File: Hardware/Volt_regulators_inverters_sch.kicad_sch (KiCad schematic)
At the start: 14 parts, among them IC1 MCP1754ST-3302E_DB, U11 LM2665M6, U12 TLV77333PDQNR, U6 TPS73133DBV, U7 TPS72325DBV, U8 TPS73201DCQ

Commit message: schematics redone, TODO: Pcb component placement
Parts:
- added C45, C46: 10 u, Capacitor_SMD:C_0603_1608Metric, symbol Device:C_Small
- IC1: footprint SOT230P700X180-4N -> mcp1754:SOT230P700X180-4N
- U12: footprint X2SON_DQN4_TEX -> tlv77333:X2SON_DQN4_TEX
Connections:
- net AVSS: now also C46.1
- net GNDA: now also C46.2
- net at U11.3 (CAP-): now also C45.2
- net at U11.6 (CAP+): now also C45.1
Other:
- note added: "3.3V LDO REG#2 e #3"
- note removed: "3.3V LDO REG#2"
- moved on the sheet: U12
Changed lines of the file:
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@@
 	(paper "A4")
+	(junction
+		(at 60.96 48.26)
+		(diameter 0)
+		(color 0 0 0 0)
+	)
 	(junction
 		(at 31.75 124.46)
@@
 	)
 	(junction
+		(at 90.17 38.1)
+		(diameter 0)
+		(color 0 0 0 0)
+	)
+	(junction
 		(at 45.72 72.39)
 		(diameter 0)
@@
 	(wire
 		(pts
+			(xy 90.17 48.26) (xy 90.17 45.72)
+		)
+		(stroke
+			(width 0)
+			(type default)
+		)
+	)
+	(wire
+		(pts
 			(xy 49.53 74.93) (xy 49.53 72.39)
 		)
@@
 	(wire
 		(pts
-			(xy 78.74 38.1) (xy 71.12 38.1)
+			(xy 78.74 45.72) (xy 71.12 45.72)
+		)
+		(stroke
+			(width 0)
+			(type default)
+		)
+	)
+	(wire
+		(pts
+			(xy 93.98 38.1) (xy 90.17 38.1)
 		)
 		(stroke
@@
 	(wire
 		(pts
+			(xy 90.17 40.64) (xy 90.17 38.1)
+		)
+		(stroke
+			(width 0)
+			(type default)
+		)
+	)
+	(wire
+		(pts
 			(xy 31.75 137.16) (xy 55.88 137.16)
 		)
@@
 	(wire
 		(pts
+			(xy 71.12 40.64) (xy 78.74 40.64)
+		)
+		(stroke
+			(width 0)
+			(type default)
+		)
+	)
+	(wire
+		(pts
 			(xy 80.01 137.16) (xy 71.12 137.16)
 		)
@@
 	(wire
 		(pts
+			(xy 90.17 38.1) (xy 71.12 38.1)
+		)
+		(stroke
+			(width 0)
+			(type default)
+		)
+	)
+	(wire
+		(pts
 			(xy 60.96 82.55) (xy 74.93 82.55)
 		)
@@
 	(wire
 		(pts
+			(xy 71.12 45.72) (xy 71.12 43.18)
+		)
+		(stroke
+			(width 0)
+			(type default)
+		)
+	)
+	(wire
+		(pts
 			(xy 31.75 124.46) (xy 45.72 124.46)
 		)
@@
 		(pts
 			(xy 74.93 80.01) (xy 74.93 82.55)
+		)
+		(stroke
+			(width 0)
+			(type default)
+		)
+	)
+	(wire
+		(pts
+			(xy 60.96 48.26) (xy 90.17 48.26)
 		)
 		(stroke
@@
 		)
 	)
-	(text "3.3V LDO REG#2\n\n"
-		(exclude_from_sim no)
-		(at 163.068 25.146 0)
+	(text "3.3V LDO REG#2 e #3\n\n\n"
+		(exclude_from_sim no)
+		(at 167.386 33.528 0)
 		(effects
 			(font
@@
 	(global_label "AVSS"
 		(shape input)
-		(at 78.74 38.1 0)
+		(at 93.98 38.1 0)
 		(fields_autoplaced yes)
 		(effects
@@
 		)
 		(property "Intersheetrefs" "${INTERSHEET_REFS}"
-			(at 86.3214 38.1 0)
+			(at 101.5614 38.1 0)
 			(effects
 				(font
@@
 	(symbol
 		(lib_id "Device:C_Small")
+		(at 78.74 43.18 0)
+		(unit 1)
+		(exclude_from_sim no)
+		(in_bom yes)
+		(on_board yes)
+		(dnp no)
+		(fields_autoplaced yes)
+		(property "Reference" "C45"
+			(at 81.28 41.9162 0)
+			(effects
+				(font
+					(size 1.27 1.27)
+				)
+				(justify left)
+			)
+		)
+		(property "Value" "10 u"
+			(at 81.28 44.4562 0)
+			(effects
+				(font
+					(size 1.27 1.27)
+				)
+				(justify left)
+			)
+		)
+		(property "Footprint" "Capacitor_SMD:C_0603_1608Metric"
+			(at 78.74 43.18 0)
+			(effects
+				(font
+					(size 1.27 1.27)
+				)
+				(hide yes)
+			)
+		)
+		(property "Datasheet" "~"
+			(at 78.74 43.18 0)
+			(effects
+				(font
+					(size 1.27 1.27)
+				)
+				(hide yes)
+			)
+		)
+		(property "Description" ""
+			(at 78.74 43.18 0)
+			(effects
+				(font
+					(size 1.27 1.27)
+				)
+				(hide yes)
+			)
+		)
+		(pin "2"
+		)
+		(pin "1"
+		)
+		(instances
+			(project "bioamplifier"
+				(path "/59c54cdb-19a2-4654-a4c9-f1907d038780/db58efb1-7103-4a17-b794-0e1a9c461960"
+					(reference "C45")
+					(unit 1)
+				)
+			)
+		)
+	)
+	(symbol
+		(lib_id "Device:C_Small")
 		(at 45.72 77.47 0)
 		(unit 1)
@@
 		(on_board yes)
 		(dnp no)
-		(fields_autoplaced yes)
 		(property "Reference" "C29"
-			(at 78.486 76.2063 0)
+			(at 73.66 75.946 0)
 			(effects
 				(font
@@
 		)
 		(property "Value" "0.1 nF"
-			(at 78.486 78.7463 0)
+			(at 72.644 79.248 0)
 			(effects
 				(font
@@
 			)
 		)
-		(property "Footprint" "SOT230P700X180-4N"
+		(property "Footprint" "mcp1754:SOT230P700X180-4N"
 			(at 196.85 136.83 0)
 			(effects
@@
 	(symbol
 		(lib_id "tlv77333:TLV77333PDQNR")
-		(at 166.37 80.01 0)
+		(at 207.01 41.91 0)
 		(unit 1)
 		(exclude_from_sim no)
@@
 		(fields_autoplaced yes)
 		(property "Reference" "U12"
-			(at 186.69 69.85 0)
+			(at 227.33 31.75 0)
 			(effects
 				(font
@@
 		)
 		(property "Value" "TLV77333PDQNR"
-			(at 186.69 72.39 0)
+			(at 227.33 34.29 0)
 			(effects
 				(font
@@
 			)
 		)
-		(property "Footprint" "X2SON_DQN4_TEX"
-			(at 166.37 80.01 0)
+		(property "Footprint" "tlv77333:X2SON_DQN4_TEX"
+			(at 207.01 41.91 0)
 			(effects
 				(font
@@
 		)
 		(property "Datasheet" "TLV77333PDQNR"
-			(at 166.37 80.01 0)
+			(at 207.01 41.91 0)
 			(effects
 				(font
@@
 		)
 		(property "Description" ""
-			(at 166.37 80.01 0)
+			(at 207.01 41.91 0)
 			(effects
 				(font
@@
 	(symbol
 		(lib_id "Device:C_Small")
+		(at 90.17 43.18 0)
+		(unit 1)
+		(exclude_from_sim no)
+		(in_bom yes)
+		(on_board yes)
+		(dnp no)
+		(fields_autoplaced yes)
+		(property "Reference" "C46"
+			(at 92.71 41.9162 0)
+			(effects
+				(font
+					(size 1.27 1.27)
+				)
+				(justify left)
+			)
+		)
+		(property "Value" "10 u"
+			(at 92.71 44.4562 0)
+			(effects
+				(font
+					(size 1.27 1.27)
+				)
+				(justify left)
+			)
+		)
+		(property "Footprint" "Capacitor_SMD:C_0603_1608Metric"
+			(at 90.17 43.18 0)
+			(effects
+				(font
+					(size 1.27 1.27)
+				)
+				(hide yes)
+			)
+		)
+		(property "Datasheet" "~"
+			(at 90.17 43.18 0)
+			(effects
+				(font
+					(size 1.27 1.27)
+				)
+				(hide yes)
+			)
+		)
+		(property "Description" ""
+			(at 90.17 43.18 0)
+			(effects
+				(font
+					(size 1.27 1.27)
+				)
+				(hide yes)
+			)
+		)
+		(pin "2"
+		)
+		(pin "1"
+		)
+		(instances
+			(project "bioamplifier"
+				(path "/59c54cdb-19a2-4654-a4c9-f1907d038780/db58efb1-7103-4a17-b794-0e1a9c461960"
+					(reference "C46")
+					(unit 1)
+				)
+			)
+		)
+	)
+	(symbol
+		(lib_id "Device:C_Small")
 		(at 147.5241 126.3073 0)
 		(unit 1)
@@
 		(on_board yes)
 		(dnp no)
-		(fields_autoplaced yes)
 		(property "Reference" "C41"
-			(at 84.836 76.2063 0)
+			(at 80.01 75.946 0)
 			(effects
 				(font
@@
 		)
 		(property "Value" "0.1 nF"
-			(at 84.836 78.7463 0)
-			(effects
-				(font
+			(at 79.756 79.248 0)
+			(effects
+				(font

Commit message: changes to pcb and schematics
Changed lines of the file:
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@@
-	(wire
-		(pts
-			(xy 230.124 119.634) (xy 230.124 119.38)
-		)
-		(stroke
-			(width 0)
-			(type default)
-		)
-	)
 	(wire
 		(pts
@@
 	(wire
 		(pts
+			(xy 220.98 119.38) (xy 231.14 119.38)
+		)
+		(stroke
+			(width 0)
+			(type default)
+		)
+	)
+	(wire
+		(pts
 			(xy 45.72 82.55) (xy 60.96 82.55)
 		)
@@
 	(wire
 		(pts
-			(xy 148.844 121.92) (xy 160.02 121.92)
-		)
-		(stroke
-			(width 0)
-			(type default)
-		)
-	)
-	(wire
-		(pts
 			(xy 45.72 72.39) (xy 45.72 74.93)
 		)
@@
 	(wire
 		(pts
-			(xy 230.632 119.634) (xy 230.124 119.634)
-		)
-		(stroke
-			(width 0)
-			(type default)
-		)
-	)
-	(wire
-		(pts
 			(xy 81.28 82.55) (xy 74.93 82.55)
 		)
@@
 		(pts
 			(xy 60.96 48.26) (xy 90.17 48.26)
-		)
-		(stroke
-			(width 0)
-			(type default)
-		)
-	)
-	(wire
-		(pts
-			(xy 230.124 119.38) (xy 220.98 119.38)
 		)
 		(stroke
@@
 		)
 	)
-	(label "5V_UNREG"
-		(at 143.51 119.38 0)
-		(fields_autoplaced yes)
-		(effects
-			(font
-				(size 1.27 1.27)
-			)
-			(justify left bottom)
-		)
-	)
-	(label "AVDD"
-		(at 148.844 121.92 0)
-		(fields_autoplaced yes)
-		(effects
-			(font
-				(size 1.27 1.27)
-			)
-			(justify left bottom)
-		)
-	)
-	(label "5V_UNREG"
-		(at 230.632 119.634 0)
-		(fields_autoplaced yes)
-		(effects
-			(font
-				(size 1.27 1.27)
-			)
-			(justify left bottom)
-		)
-	)
 	(global_label "3.3V_UNREG"
 		(shape input)
@@
 		)
 	)
+	(global_label "5V_UNREG"
+		(shape input)
+		(at 231.14 119.38 0)
+		(fields_autoplaced yes)
+		(effects
+			(font
+				(size 1.27 1.27)
+			)
+			(justify left)
+		)
+		(property "Intersheetrefs" "${INTERSHEET_REFS}"
+			(at 243.7409 119.38 0)
+			(effects
+				(font
+					(size 1.27 1.27)
+				)
+				(justify left)
+				(hide yes)
+			)
+		)
+	)
 	(global_label "DVDD"
 		(shape input)
@@
 		)
 	)
+	(global_label "AVDD"
+		(shape input)
+		(at 160.02 121.92 180)
+		(fields_autoplaced yes)
+		(effects
+			(font
+				(size 1.27 1.27)
+			)
+			(justify right)
+		)
+		(property "Intersheetrefs" "${INTERSHEET_REFS}"
+			(at 152.3176 121.92 0)
+			(effects
+				(font
+					(size 1.27 1.27)
+				)
+				(justify right)
+				(hide yes)
+			)
+		)
+	)
 	(global_label "-2.5V_UNREG"
 		(shape input)
@@
 				(hide yes)
 			)
+		)
+	)
+	(global_label "5V_UNREG"
+		(shape input)
+		(at 143.51 119.38 180)
+		(fields_autoplaced yes)
+		(effects
+			(font
+				(size 1.27 1.27)
+			)
+			(justify right)
+		)
+		(property "Intersheetrefs" "${INTERSHEET_REFS}"
+			(at 130.9091 119.38 0)
+			(effects
+				(font
+					(size 1.27 1.27)
+				)
+				(justify right)
+				(hide yes)
+			)

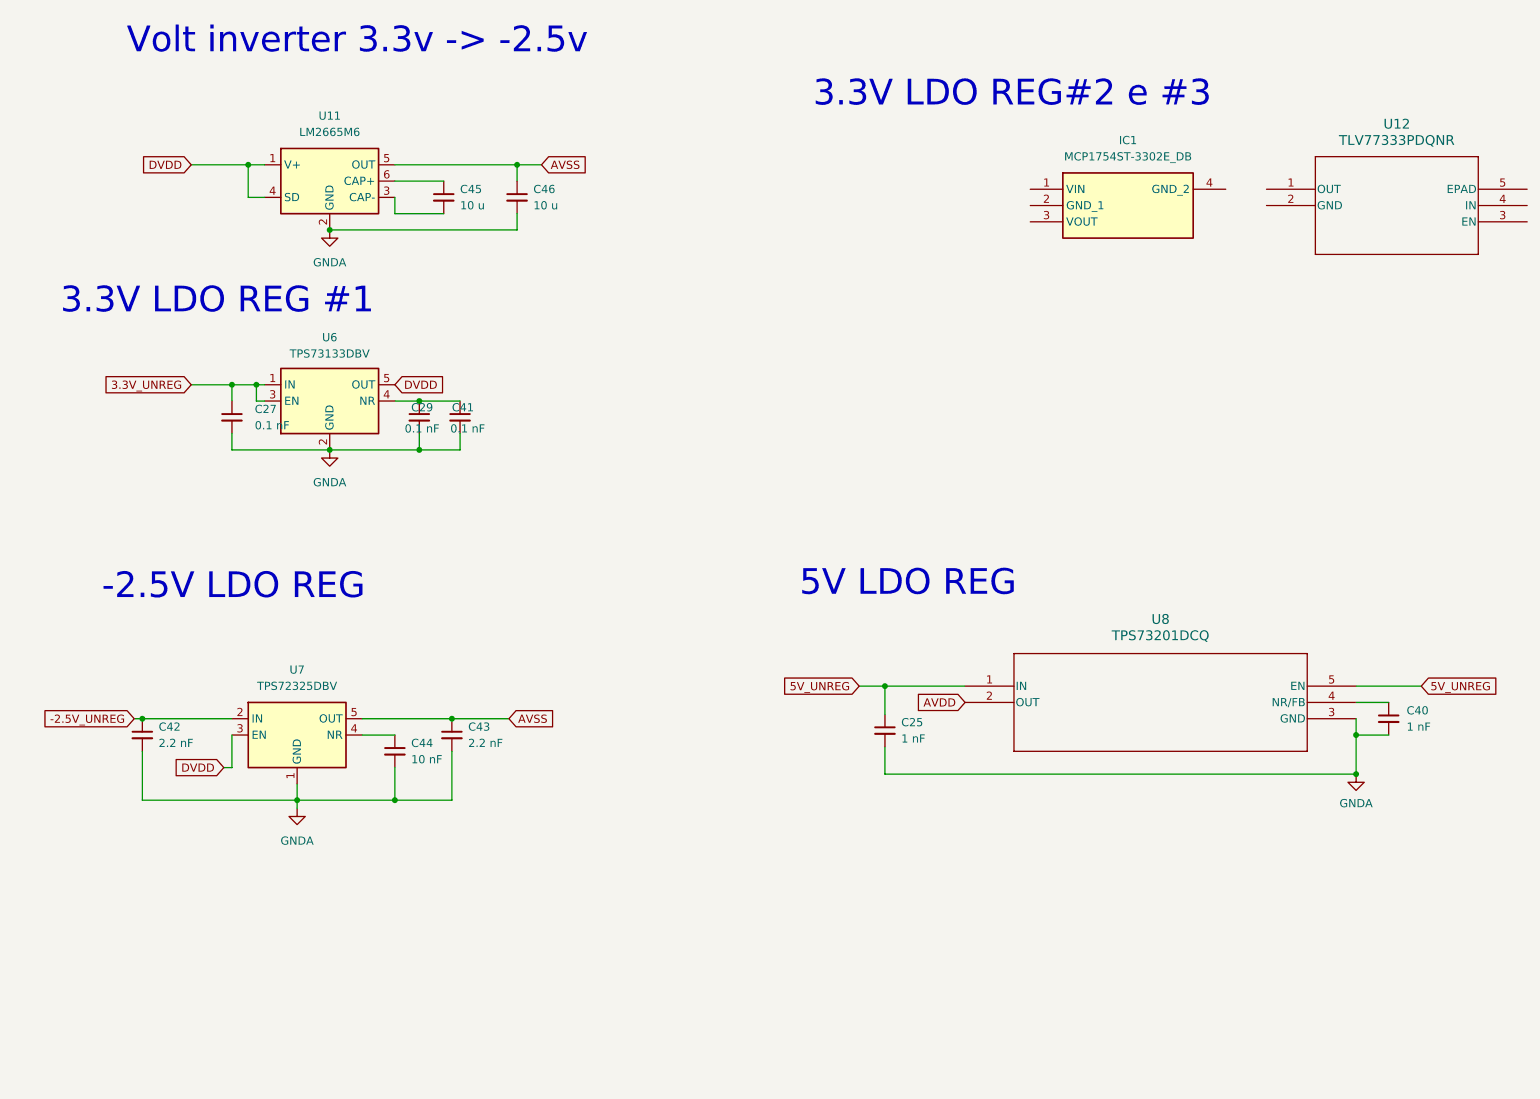
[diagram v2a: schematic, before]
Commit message: removed 5V LDO Regulator
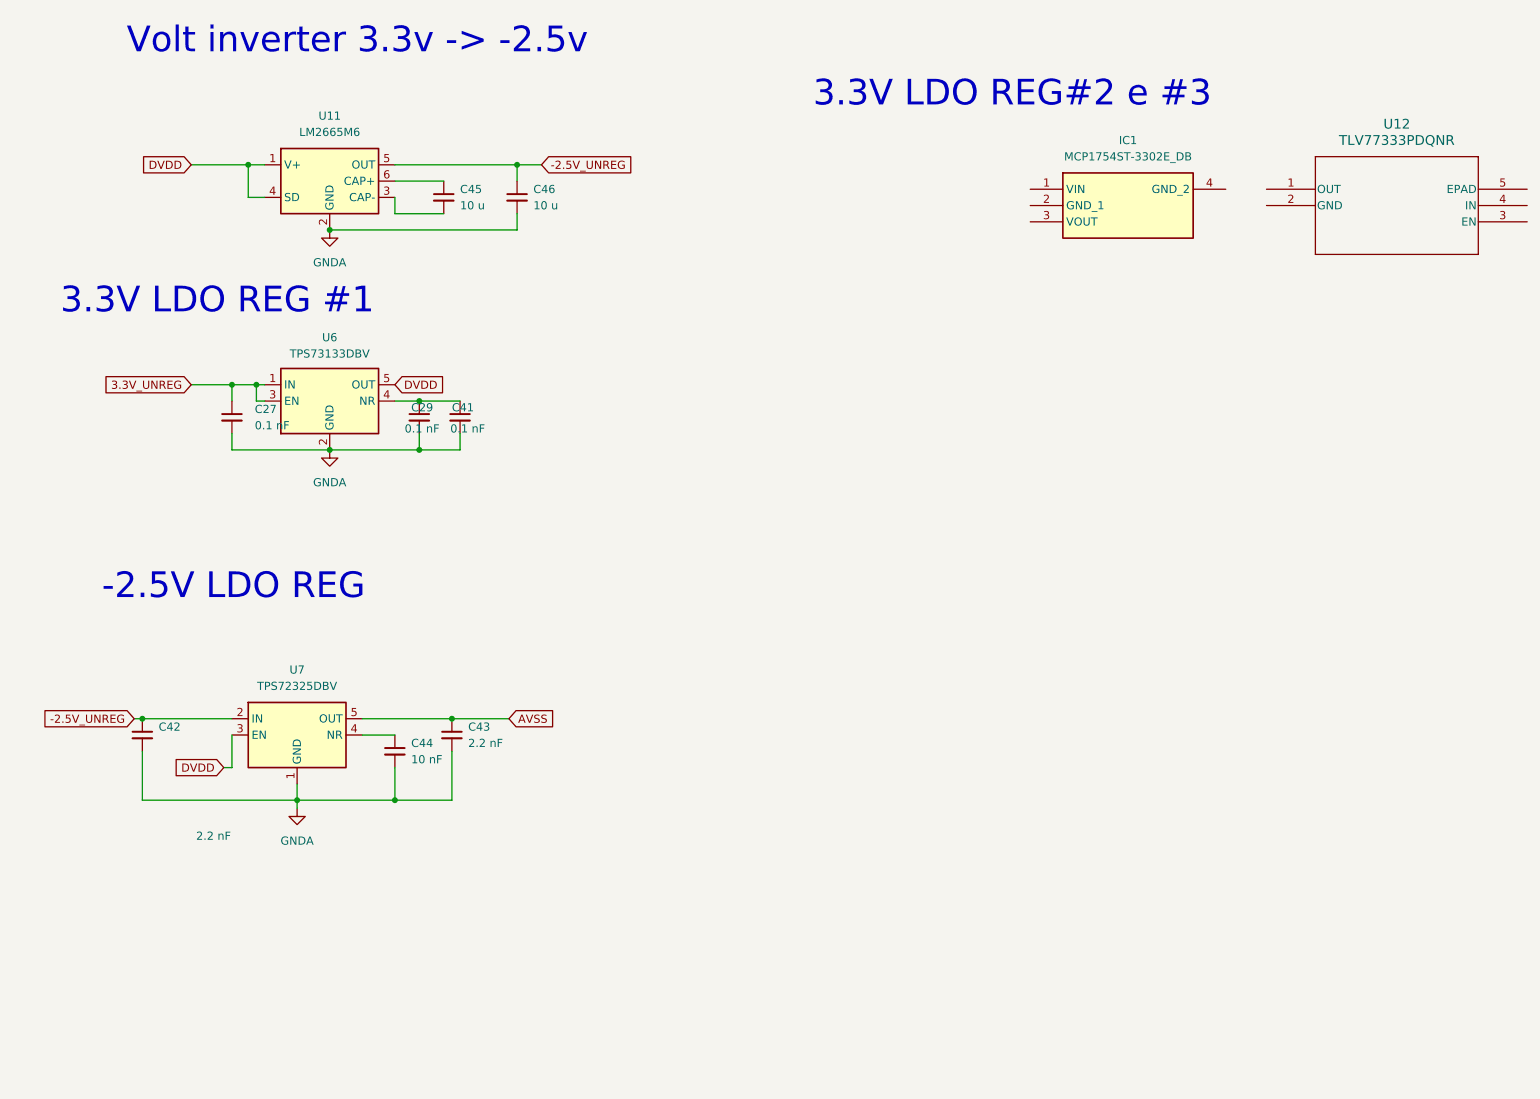
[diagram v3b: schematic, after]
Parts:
- removed C25, C40: 1 nF, Capacitor_SMD:C_0603_1608Metric, symbol Device:C_Small
- removed U8: TPS73201DCQ, tps732:DCQ6_TEX, symbol tps732:TPS73201DCQ
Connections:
- net -2.5V_UNREG: now also C46.1, U11.5 (OUT)
- net AVSS: no longer C46.1, U11.5 (OUT)
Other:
- note removed: "5V LDO REG"

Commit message: power pin layout change
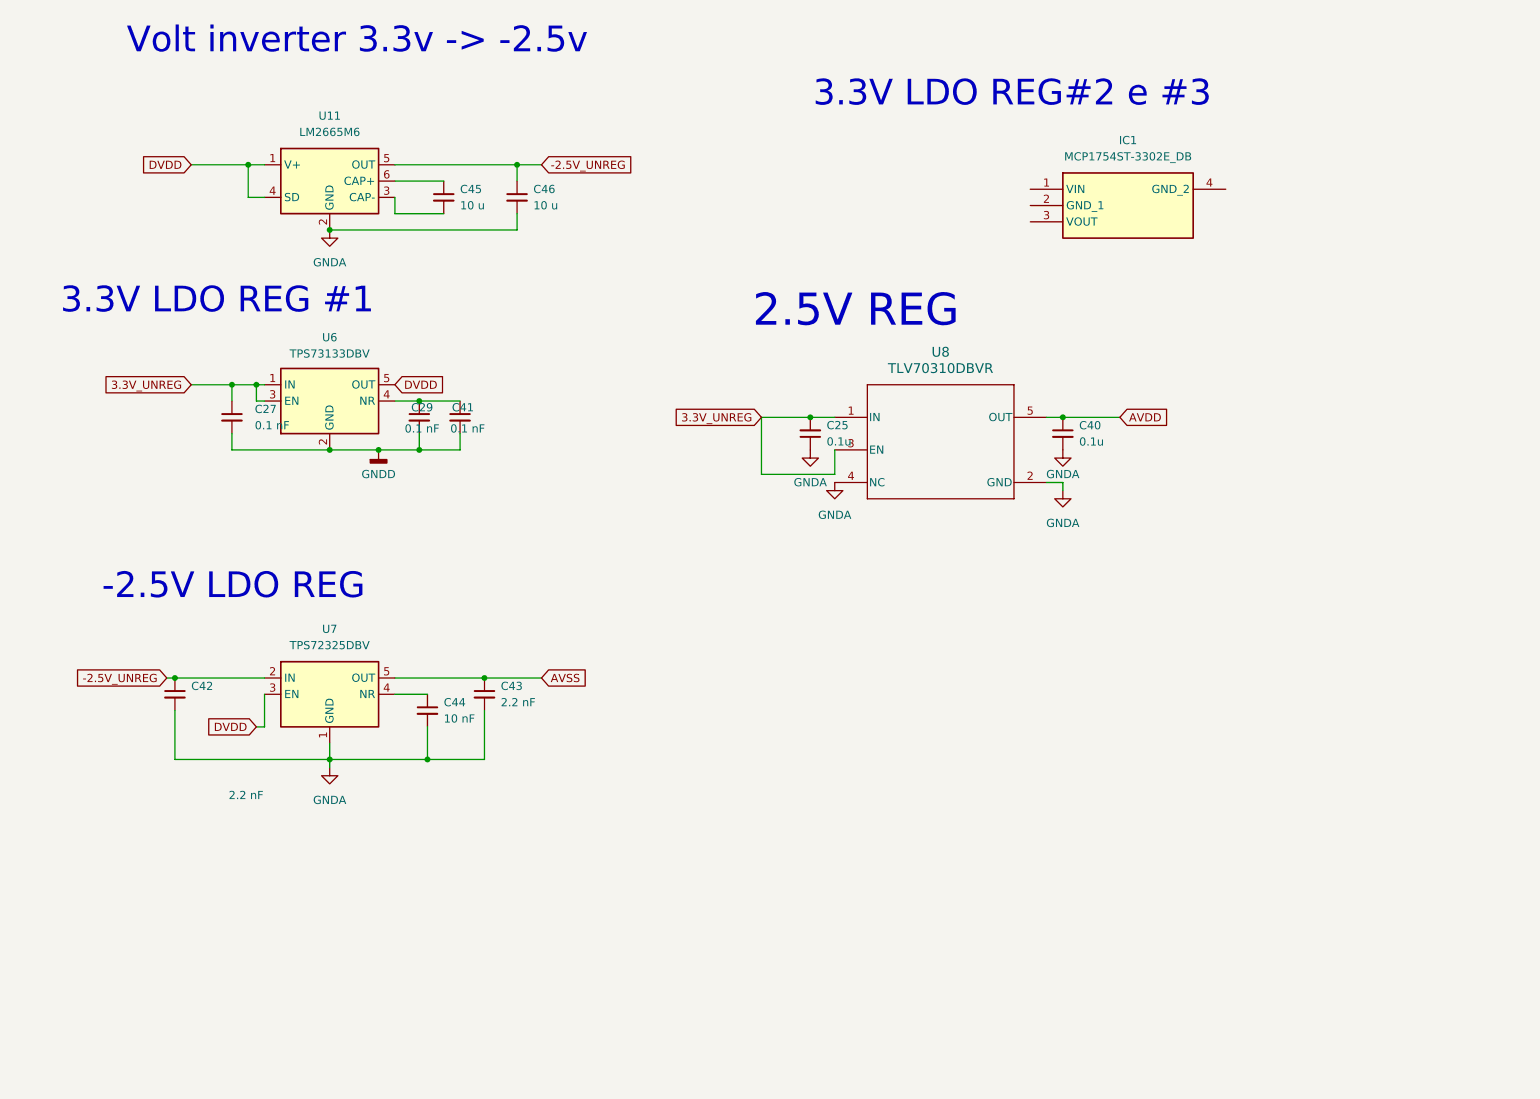
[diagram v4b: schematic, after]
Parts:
- removed U12: TLV77333PDQNR, tlv77333:X2SON_DQN4_TEX, symbol tlv77333:TLV77333PDQNR
- added C25, C40: 0.1u, Capacitor_SMD:C_0603_1608Metric, symbol Device:C_Small
- added U8: TLV70310DBVR, DBV0005A-IPC_A, symbol tlv703:TLV70310DBVR
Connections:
- net 3.3V_UNREG: now also C25.2, U8.1 (IN), U8.3 (EN)
- net GNDA: now also C25.1, C40.2, U8.2 (GND), U8.4 (NC); no longer C27.2, C29.2, C41.2, U6.2 (GND)
- new net AVDD: C40.1, U8.5 (OUT)
- new net GNDD: C27.2, C29.2, C41.2, U6.2 (GND)
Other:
- note added: "2.5V REG"
- moved on the sheet: C42, C43, C44, U7

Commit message: Fix Last DRC Errors
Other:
- note added: "2.5V LDO REG"
- note removed: "2.5V REG"
- moved on the sheet: C25, C40, U8

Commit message: Add Fiducials, Mounting holes, 3d models
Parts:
- U8: footprint DBV0005A-IPC_A -> tlv702:DBV0005A-IPC_A
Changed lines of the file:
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@@
 			)
 		)
-		(property "Footprint" "DBV0005A-IPC_A"
+		(property "Footprint" "tlv702:DBV0005A-IPC_A"
 			(at 39.37 163.83 0)
 			(effects
